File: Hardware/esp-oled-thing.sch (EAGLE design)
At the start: 43 parts, among them Q1 2.5A/30V, U1 MCP73831, U2 TPS61200

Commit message: Initial layout started.
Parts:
- added GND: TPTP10R, testpad:TPTP10R
- renumbered SJ1 to CHARGER_STATUS, SJ2 to TPS_EN, SJ3 to GPIO2_GND, SJ4 to SMPS_GND
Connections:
- net GND: now also GND.TP
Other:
- note added: "Battery Connector"
- note added: "Power Switch"
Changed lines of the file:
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@@
 <?xml version="1.0" encoding="utf-8"?>
 <!DOCTYPE eagle SYSTEM "eagle.dtd">
-<eagle version="7.3.0">
+<eagle version="6.2">
 <drawing>
 <settings>
@@
 <part name="R12" library="adafruit" deviceset="R-US_" device="M0805" value="10K"/>
 <part name="GND3" library="supply1" deviceset="GND" device=""/>
-<part name="SJ1" library="SparkFun" deviceset="SOLDERJUMPER" device="NO"/>
+<part name="CHARGER_STATUS" library="SparkFun" deviceset="SOLDERJUMPER" device="NO"/>
 <part name="R14" library="adafruit" deviceset="R-US_" device="M0805" value="4.7K"/>
 <part name="R15" library="adafruit" deviceset="R-US_" device="M0805" value="4.7K"/>
 <part name="GND6" library="supply1" deviceset="GND" device=""/>
 <part name="R16" library="adafruit" deviceset="R-US_" device="M0805" value="10K"/>
-<part name="SJ2" library="SparkFun" deviceset="SOLDERJUMPER" device="NO"/>
-<part name="SJ3" library="SparkFun" deviceset="SOLDERJUMPER" device="NO"/>
+<part name="TPS_EN" library="SparkFun" deviceset="SOLDERJUMPER" device="NO"/>
+<part name="GPIO2_GND" library="SparkFun" deviceset="SOLDERJUMPER" device="NO"/>
 <part name="GND7" library="supply1" deviceset="GND" device=""/>
-<part name="SJ4" library="SparkFun" deviceset="SOLDERJUMPER" device="NO"/>
+<part name="SMPS_GND" library="SparkFun" deviceset="SOLDERJUMPER" device="NO"/>
 <part name="GND15" library="SparkFun" deviceset="GND" device=""/>
 <part name="SJ5" library="jumper" deviceset="SJ2W" device=""/>
 <part name="S1" library="switch" deviceset="TL39PO" device=""/>
 <part name="P+5" library="SparkFun" deviceset="VCC" device=""/>
+<part name="GND" library="testpad" deviceset="TP" device="TP10R">
+<attribute name="TP_SIGNAL_NAME" value=""/>
+</part>
+<part name="GND16" library="supply1" deviceset="GND" device=""/>
 </parts>
 <sheets>
@@
 <text x="152.4" y="55.88" size="1.778" layer="97">Li-Po battery Charger Section</text>
 <text x="30.48" y="109.22" size="1.778" layer="97">The Power Supply Regulator for the System</text>
-<wire x1="2.54" y1="175.26" x2="139.7" y2="175.26" width="0.1524" layer="97"/>
+<wire x1="2.54" y1="175.26" x2="88.9" y2="175.26" width="0.1524" layer="97"/>
 <text x="114.3" y="-10.16" size="1.778" layer="97">Solder jumper for connecting vref to vcc</text>
+<wire x1="88.9" y1="175.26" x2="129.54" y2="175.26" width="0.1524" layer="97"/>
+<wire x1="129.54" y1="175.26" x2="139.7" y2="175.26" width="0.1524" layer="97"/>
 <wire x1="139.7" y1="104.14" x2="2.54" y2="104.14" width="0.1524" layer="97"/>
 <wire x1="142.24" y1="177.8" x2="142.24" y2="175.26" width="0.1524" layer="97"/>
@@
 <wire x1="139.7" y1="91.44" x2="139.7" y2="104.14" width="0.1524" layer="97"/>
 <text x="233.68" y="86.36" size="1.778" layer="95">optional load sharing circuit</text>
+<wire x1="88.9" y1="175.26" x2="88.9" y2="152.4" width="0.1524" layer="97"/>
+<wire x1="88.9" y1="152.4" x2="129.54" y2="152.4" width="0.1524" layer="97"/>
+<wire x1="129.54" y1="152.4" x2="129.54" y2="175.26" width="0.1524" layer="97"/>
+<wire x1="27.94" y1="99.06" x2="27.94" y2="76.2" width="0.1524" layer="97"/>
+<wire x1="27.94" y1="76.2" x2="76.2" y2="76.2" width="0.1524" layer="97"/>
+<wire x1="76.2" y1="76.2" x2="76.2" y2="99.06" width="0.1524" layer="97"/>
+<wire x1="76.2" y1="99.06" x2="27.94" y2="99.06" width="0.1524" layer="97"/>
+<text x="40.64" y="96.52" size="1.778" layer="97">Power Switch</text>
+<text x="99.06" y="172.72" size="1.778" layer="97">Battery Connector</text>
 </plain>
 <instances>
@@
 </instance>
 <instance part="GND3" gate="1" x="238.76" y="60.96"/>
-<instance part="SJ1" gate="1" x="170.18" y="111.76" smashed="yes">
+<instance part="CHARGER_STATUS" gate="1" x="170.18" y="111.76" smashed="yes">
 <attribute name="NAME" x="167.64" y="114.3" size="1.778" layer="95"/>
 </instance>
@@
 <attribute name="VALUE" x="183.642" y="153.67" size="1.778" layer="96" rot="R90"/>
 </instance>
-<instance part="SJ2" gate="1" x="238.76" y="121.92" smashed="yes">
+<instance part="TPS_EN" gate="1" x="238.76" y="121.92" smashed="yes">
 <attribute name="NAME" x="236.22" y="124.46" size="1.778" layer="95"/>
 </instance>
-<instance part="SJ3" gate="1" x="236.22" y="104.14" smashed="yes" rot="R90">
+<instance part="GPIO2_GND" gate="1" x="236.22" y="104.14" smashed="yes" rot="R90">
 <attribute name="NAME" x="233.68" y="101.6" size="1.778" layer="95" rot="R90"/>
 </instance>
 <instance part="GND7" gate="1" x="236.22" y="93.98"/>
-<instance part="SJ4" gate="1" x="15.24" y="116.84" smashed="yes" rot="R90">
+<instance part="SMPS_GND" gate="1" x="15.24" y="116.84" smashed="yes" rot="R90">
 <attribute name="NAME" x="12.7" y="114.3" size="1.778" layer="95" rot="R90"/>
 </instance>
@@
 <instance part="S1" gate="BEF1" x="53.34" y="86.36" rot="R270"/>
 <instance part="P+5" gate="1" x="71.12" y="91.44"/>
+<instance part="GND" gate="G$1" x="119.38" y="162.56" smashed="yes">
+<attribute name="NAME" x="120.65" y="163.83" size="1.778" layer="95" rot="R90"/>
+<attribute name="TP_SIGNAL_NAME" x="120.65" y="161.29" size="1.778" layer="97"/>
+</instance>
+<instance part="GND16" gate="1" x="119.38" y="157.48"/>
 </instances>
 <busses>
@@
 </segment>
 <segment>
-<pinref part="SJ3" gate="1" pin="1"/>
+<pinref part="GPIO2_GND" gate="1" pin="1"/>
 <pinref part="GND7" gate="1" pin="GND"/>
 <wire x1="236.22" y1="99.06" x2="236.22" y2="96.52" width="0.1524" layer="91"/>
 </segment>
 <segment>
-<pinref part="SJ4" gate="1" pin="1"/>
+<pinref part="SMPS_GND" gate="1" pin="1"/>
 <pinref part="GND15" gate="1" pin="GND"/>
 <wire x1="15.24" y1="109.22" x2="15.24" y2="111.76" width="0.1524" layer="91"/>
+</segment>
+<segment>
+<pinref part="GND" gate="G$1" pin="TP"/>
+<pinref part="GND16" gate="1" pin="GND"/>
 </segment>
 </net>
@@
 <junction x="210.82" y="132.08"/>
 <pinref part="I2C_OLED" gate="G$1" pin="4"/>
-<pinref part="SJ3" gate="1" pin="2"/>
+<pinref part="GPIO2_GND" gate="1" pin="2"/>
 <wire x1="228.6" y1="114.3" x2="236.22" y2="114.3" width="0.1524" layer="91"/>
 <wire x1="236.22" y1="114.3" x2="236.22" y2="109.22" width="0.1524" layer="91"/>
@@
 <junction x="25.4" y="121.92"/>
 <junction x="38.1" y="121.92"/>
-<pinref part="SJ4" gate="1" pin="2"/>
+<pinref part="SMPS_GND" gate="1" pin="2"/>
 </segment>
 </net>
@@
 </segment>
 <segment>
-<pinref part="SJ2" gate="1" pin="2"/>
+<pinref part="TPS_EN" gate="1" pin="2"/>
 <wire x1="243.84" y1="121.92" x2="251.46" y2="121.92" width="0.1524" layer="91"/>
 <wire x1="251.46" y1="121.92" x2="251.46" y2="134.62" width="0.1524" layer="91"/>
@@
 </segment>
 <segment>
-<pinref part="SJ1" gate="1" pin="1"/>
+<pinref part="CHARGER_STATUS" gate="1" pin="1"/>
 <wire x1="165.1" y1="111.76" x2="162.56" y2="111.76" width="0.1524" layer="91"/>
 <label x="162.56" y="104.14" size="1.778" layer="95" rot="R180"/>
@@
 <net name="N$1" class="0">
 <segment>
-<pinref part="SJ1" gate="1" pin="2"/>
+<pinref part="CHARGER_STATUS" gate="1" pin="2"/>
 <pinref part="U$2" gate="G$1" pin="GPIO13"/>
 <wire x1="175.26" y1="111.76" x2="190.5" y2="111.76" width="0.1524" layer="91"/>
@@
 <segment>
 <pinref part="U$2" gate="G$1" pin="GPIO4"/>
-<pinref part="SJ2" gate="1" pin="1"/>
+<pinref part="TPS_EN" gate="1" pin="1"/>
 <wire x1="223.52" y1="121.92" x2="233.68" y2="121.92" width="0.1524" layer="91"/>
 </segment>

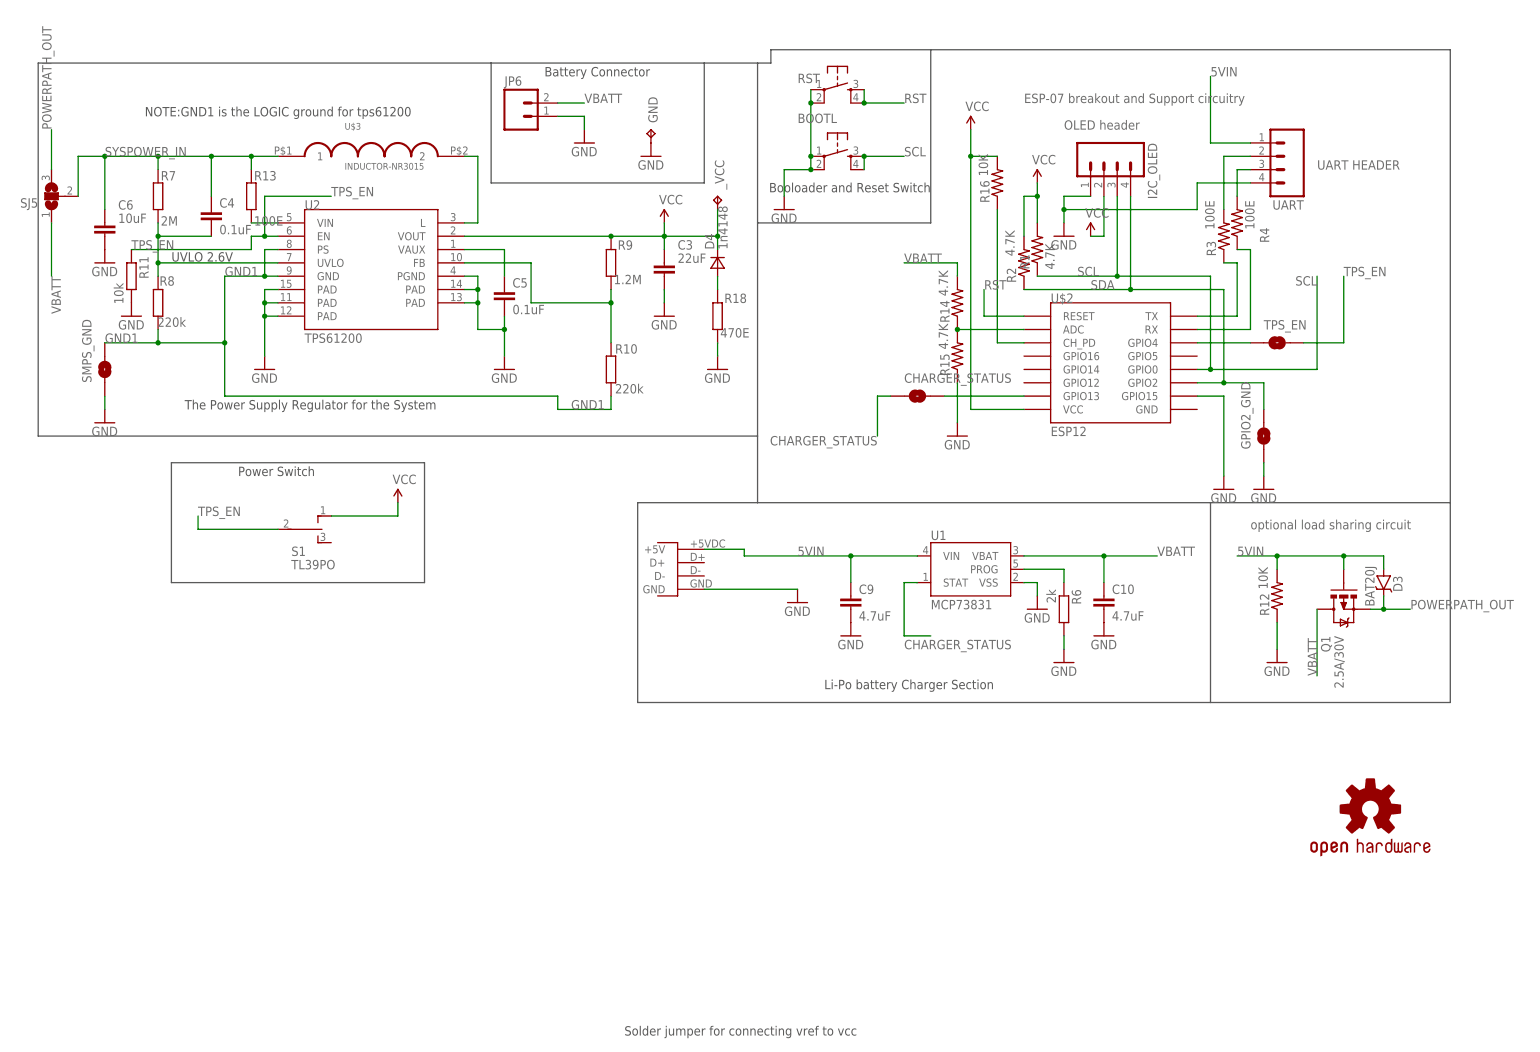
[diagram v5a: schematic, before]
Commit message: layout and components modified for better solderability.
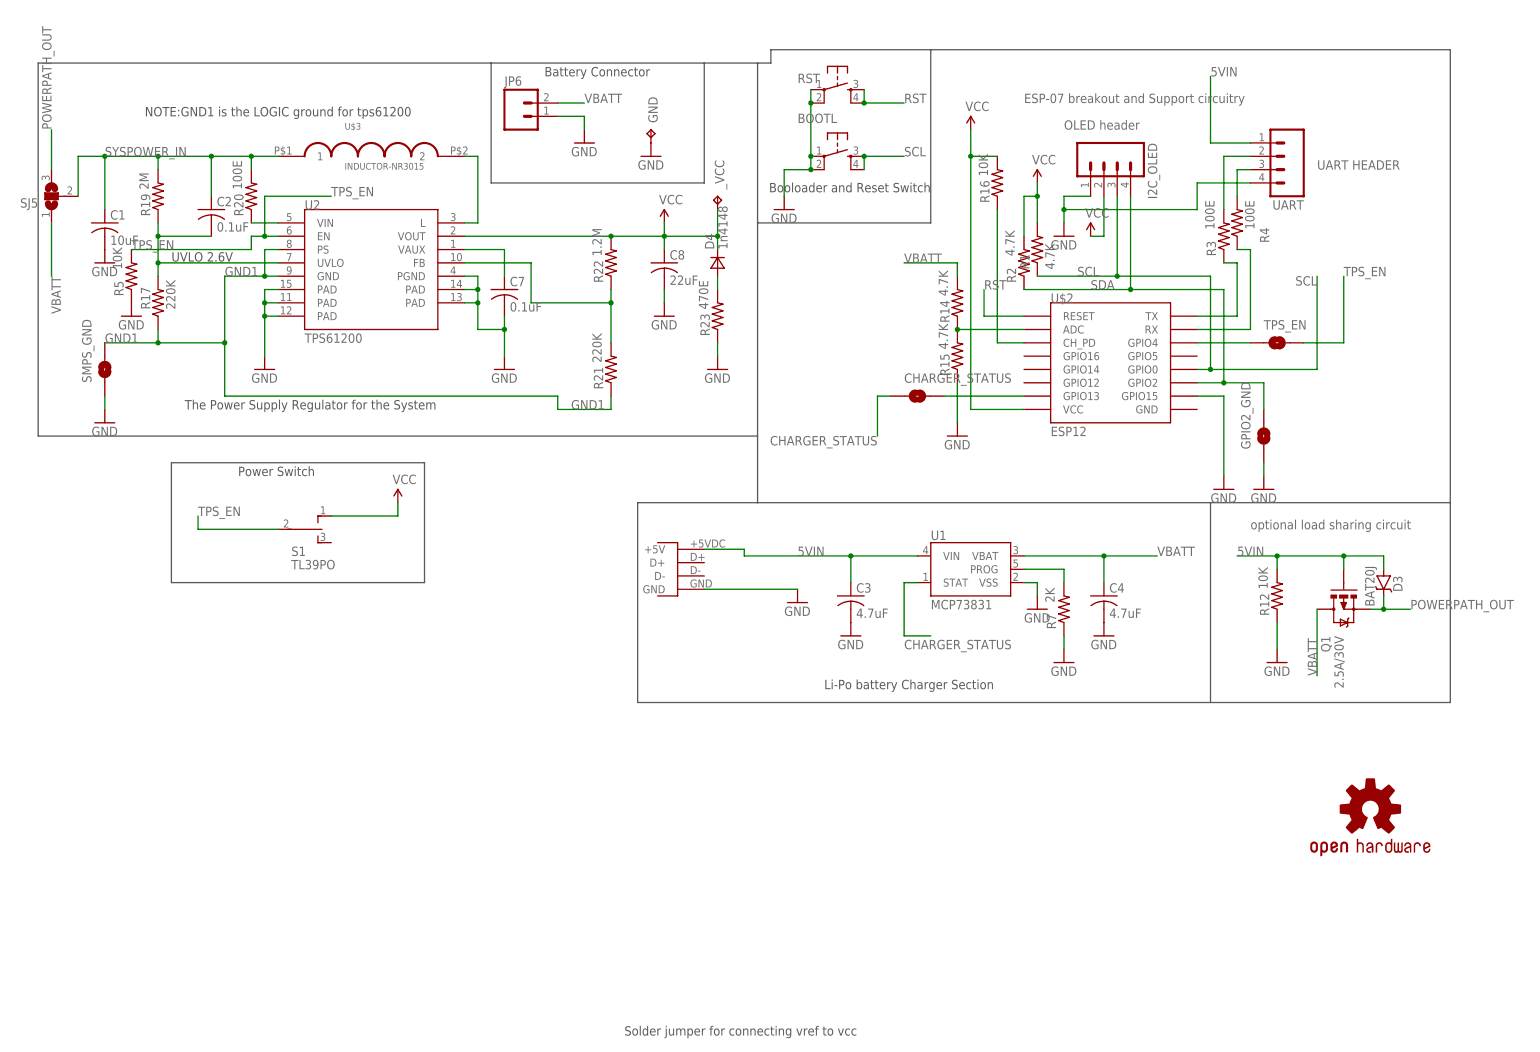
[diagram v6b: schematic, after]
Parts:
- removed C10, C9: 4.7uF, rcl:C-EUC0603K
- removed C5: 0.1uF, rcl:C-EUC0402
- removed C6: 10uF, rcl:C-EUC0805
- removed R10, R8: 220k, rcl:R-EU_R0402
- removed R11: 10k, rcl:R-EU_R0402
- removed R13: 100E, rcl:R-EU_R0402
- removed R18: 470E, rcl:R-EU_R0402
- removed R6: 2k, rcl:R-EU_R0402
- removed R9: 1.2M, rcl:R-EU_R0402
- added C1: 10uF, rcl:C-USC0805
- added C2, C7: 0.1uF, rcl:C-USC0805
- added C8: 22uF, rcl:C-USC0805
- added R17, R21: 220K, adafruit:R-US_M0805
- added R19: 2M, adafruit:R-US_M0805
- added R20: 100E, adafruit:R-US_M0805
- added R22: 1.2M, adafruit:R-US_M0805
- added R23: 470E, adafruit:R-US_M0805
- added R5: 10K, adafruit:R-US_M0805
- C3: value 22uF -> 4.7uF; device rcl:C-EUC0603K -> rcl:C-USC0805
- C4: value 0.1uF -> 4.7uF; device rcl:C-EUC0402 -> rcl:C-USC0805
- R7: value 2M -> 2K; device rcl:R-EU_R0402 -> adafruit:R-US_M0805
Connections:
- net 5VIN: now also C3.1; no longer C9.1
- net FB: now also R21.2, R22.1; no longer R10.2, R9.1
- net GND: now also C1.2, C4.2, C7.2, C8.2, R23.1, R5.1, R7.1; no longer C10.2, C5.2, C6.2, C9.2, R11.2, R18.1, R6.2
- net GND1: now also R17.1, R21.1; no longer R10.1, R8.1
- net N$13: now also R7.2; no longer R6.1
- net N$18: now also C7.1; no longer C5.1
- net N$21: now also R23.2; no longer R18.2
- net SYSPOWER_IN: now also C1.1, C2.1, R19.2, R20.2; no longer C4.1, C6.1, R13.2, R7.2
- net TPS_EN: now also R5.2; no longer R11.1
- net UVLO: now also C2.2, R17.2, R19.1; no longer C4.2, R7.1, R8.2
- net VBATT: now also C4.1; no longer C10.1
- net VCC: now also C8.1, R22.2; no longer C3.1, R9.2
- net VIN: now also R20.1; no longer R13.1
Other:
- moved on the sheet: C3, C4
